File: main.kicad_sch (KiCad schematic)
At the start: 19 parts, among them J1 Conn_01x02_Pin, U1 LMC555xCMX, U2 LT8374RUFM-WPBF

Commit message: values
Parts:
- removed J1: Conn_01x02_Pin, symbol Connector:Conn_01x02_Pin
- added C10, C11, C8: C, symbol Device:C
- added C9: C_Polarized_US, symbol Device:C_Polarized_US
- added U3: TPS7B8133QDGNRQ1, VSSOP8_DGN_TEX, symbol _TPS7B81-Q1:TPS7B8133QDGNRQ1
- L1: value L -> 150 uH; Mfr (none) -> Bourns Inc.; Mfr P/N (none) -> SRN1060-151M; Supplier_1 (none) -> DigiKey; Supplier_1 P/N (none) -> SRN1060-151MCT-ND; Supplier_1 Price @ Qty (none) -> $0.67; Supplier_1 Unit Price (none) -> $0.67000
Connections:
- net GND: now also U2.8 (GND), C10.2, C11.2, C8.2, C9.2, U3.4 (GND), U3.5 (GND), U3.6 (GND), U3.9 (EPAD)
- net VIN: now also C8.1, C9.1
- net signal: now also U2.5 (CTRL)
- net DRV renamed +3V3
- net +3V3: now also C11.1, U3.8 (OUT)
- new net: C10.1, U3.1 (IN), U3.2 (EN)
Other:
- moved on the sheet: C1, C2, C3, C4, C5, C6, C7, D1, D2, D3, L1, R1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

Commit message: values, footprints, and part info complete
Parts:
- added C12: 1uF, Capacitor_SMD:C_0603_1608Metric, symbol Device:C
- added D4, D5: LED, _NavLights:LED_JB3030AWT_3X3_CRE, symbol Device:LED
- C1: value C -> 22nf; footprint (none) -> Capacitor_SMD:C_0805_2012Metric; Mfr (none) -> Murata Electronics; Mfr P/N (none) -> GCM21B5C1H223FA16L; Supplier_1 (none) -> DigiKey; Supplier_1 P/N (none) -> 490-GCM21B5C1H223FA16LCT-ND; Supplier_1 Price @ Qty (none) -> 1; Supplier_1 Unit Price (none) -> $0.52
- C10, C11, C8: value C -> 10uF; footprint (none) -> Capacitor_SMD:C_0805_2012Metric; Mfr (none) -> Murata Electronics; Mfr P/N (none) -> GRM21BR61H106KE43L; Supplier_1 (none) -> DigiKey; Supplier_1 P/N (none) -> 490-18663-1-ND; Supplier_1 Price @ Qty (none) -> 1; Supplier_1 Unit Price (none) -> $0.28
- C2, C4: footprint (none) -> Capacitor_SMD:C_0603_1608Metric; Mfr (none) -> KEMET; Mfr P/N (none) -> C0603C104K5RACTU; Supplier_1 (none) -> DigiKey; Supplier_1 P/N (none) -> 399-C0603C104K5RACTUCT-ND; Supplier_1 Price @ Qty (none) -> 1; Supplier_1 Unit Price (none) -> $0.08
- C3: value C -> 0.27; footprint (none) -> Capacitor_SMD:C_0805_2012Metric; Mfr (none) -> YAGEO; Mfr P/N (none) -> CC0805KKX7R9BB274; Supplier_1 (none) -> DigiKey; Supplier_1 P/N (none) -> 13-CC0805KKX7R9BB274CT-ND; Supplier_1 Price @ Qty (none) -> 1; Supplier_1 Unit Price (none) -> $0.20
- C5: value C -> 4.7uF; footprint (none) -> Capacitor_SMD:C_0805_2012Metric; Mfr (none) -> Murata Electronics; Mfr P/N (none) -> GRM21BR61H475KE51L; Supplier_1 (none) -> DigiKey; Supplier_1 P/N (none) -> 490-10751-1-ND; Supplier_1 Price @ Qty (none) -> 1; Supplier_1 Unit Price (none) -> $0.19
- C6: value C -> 47pF; footprint (none) -> Capacitor_SMD:C_0603_1608Metric; Mfr (none) -> Vishay Vitramon; Mfr P/N (none) -> VJ0603A470FXACW1BC; Supplier_1 (none) -> DigiKey; Supplier_1 P/N (none) -> 720-VJ0603A470FXACW1BCCT-ND; Supplier_1 Price @ Qty (none) -> 1; Supplier_1 Unit Price (none) -> $0.13
- C7: value C -> 2.2uF; footprint (none) -> Capacitor_SMD:C_0603_1608Metric; Mfr (none) -> Murata Electronics; Mfr P/N (none) -> GRM188R61H225KE11D; Supplier_1 (none) -> DigiKey; Supplier_1 P/N (none) -> 490-10733-1-ND; Supplier_1 Price @ Qty (none) -> 1; Supplier_1 Unit Price (none) -> $0.25
- C9: value C_Polarized_US -> 47uF; footprint (none) -> _NavLights:CAP_EEEFN2A100L; Mfr (none) -> Chemi-Con; Mfr P/N (none) -> HHXC500ARA470MHA0G; Supplier_1 (none) -> DigiKey; Supplier_1 P/N (none) -> 565-HHXC500ARA470MHA0GCT-ND; Supplier_1 Price @ Qty (none) -> 1; Supplier_1 Unit Price (none) -> $1.09
- D1, D2, D3: footprint (none) -> _NavLights:LED_JB3030AWT_3X3_CRE; Supplier_1 (none) -> DigiKey; Supplier_1 P/N (none) -> 2138-JB3030AWT-P-H65EA0000-N0000001CT-ND; Supplier_1 Price @ Qty (none) -> $0.69 for 10; Supplier_1 Unit Price (none) -> $0.10
- L1: value 150 uH -> 150uH; footprint (none) -> _NavLights:IND_BOURNS_SRN1060
- R1: value R_US -> 274kOhm; footprint (none) -> Resistor_SMD:R_0603_1608Metric; Mfr (none) -> Panasonic Electronic Components; Mfr P/N (none) -> ERA-3AEB2743V; Supplier_1 (none) -> DigiKey; Supplier_1 P/N (none) -> P274KDBCT-ND; Supplier_1 Price @ Qty (none) -> 1; Supplier_1 Unit Price (none) -> $0.10
- R2: value 1k -> 2490kOHm; footprint (none) -> Resistor_SMD:R_0603_1608Metric; Mfr (none) -> Stackpole Electronics Inc; Mfr P/N (none) -> RMCF0603FT2M49; Supplier_1 (none) -> DigKey; Supplier_1 P/N (none) -> RMCF0603FT2M49CT-ND; Supplier_1 Price @ Qty (none) -> 1; Supplier_1 Unit Price (none) -> $0.10
- R3: value R_US -> 100kOHm; footprint (none) -> Resistor_SMD:R_0603_1608Metric; Mfr (none) -> Stackpole Electronics Inc; Mfr P/N (none) -> RMCF0603FT100K; Supplier_1 (none) -> DigiKey; Supplier_1 P/N (none) -> RMCF0603FT100KCT-ND; Supplier_1 Price @ Qty (none) -> 1; Supplier_1 Unit Price (none) -> $0.10
- R4: value R_US -> 24mO; footprint (none) -> Resistor_SMD:R_0805_2012Metric; Mfr (none) -> Panasonic Electronic Components; Mfr P/N (none) -> ERJ-6CWDR024V; Supplier_1 (none) -> DigiKey; Supplier_1 P/N (none) -> P124410CT-ND; Supplier_1 Price @ Qty (none) -> 1; Supplier_1 Unit Price (none) -> $0.61
- R5: value R_US -> 10kO; footprint (none) -> Resistor_SMD:R_0603_1608Metric; Mfr (none) -> Panasonic Electronic Components; Mfr P/N (none) -> ERA-3AEB103V; Supplier_1 (none) -> DigiKey; Supplier_1 P/N (none) -> P10KDBCT-ND; Supplier_1 Price @ Qty (none) -> 1; Supplier_1 Unit Price (none) -> $0.10
- U2: Mfr (none) -> Analog Devices Inc.; Mfr P/N (none) -> LT8374RUFM#WPBF; Supplier_1 (none) -> DigiKey; Supplier_1 P/N (none) -> 505-LT8374RUFM#WPBF-ND; Supplier_1 Price @ Qty (none) -> 1; Supplier_1 Unit Price (none) -> $5.34
- U3: Mfr (none) -> Texas Instruments; Mfr P/N (none) -> TPS7B8133QDGNRQ1; Supplier_1 (none) -> DigiKey; Supplier_1 P/N (none) -> 296-TPS7B8133QDGNRQ1CT-ND; Supplier_1 Price @ Qty (none) -> 1; Supplier_1 Unit Price (none) -> $1.60
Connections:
- net GND: now also U2.17 (EPAD), C12.2, D5.1 (K)
- net INTVCC: now also U2.1 (SYNC/SPRD), U2.6 (CAP)
- net VIN: now also C10.1, U3.1 (IN), U3.2 (EN), C12.1
- net at D3.1 (K): now also D4.2 (A)
- new net: D4.1 (K), D5.2 (A)
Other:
- moved on the sheet: C1, C11, C2, C3, C4, C5, C6, C7, C8, C9, D1, L1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

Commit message: imprv to layout
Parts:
- added VIN: TestPoint, MountingHole:MountingHole_6mm_Pad_TopBottom, symbol Connector:TestPoint
- U3: footprint VSSOP8_DGN_TEX -> _NavLights:VSSOP8_DGN_TEX
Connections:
- net VIN: now also VIN.1
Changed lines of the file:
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@@
 			)
 		)
-		(property "Footprint" "VSSOP8_DGN_TEX"
+		(property "Footprint" "_NavLights:VSSOP8_DGN_TEX"
 			(at 58.42 48.26 0)
 			(effects
@@
 					(unit 1)
 				)
+			)
+		)
+	)
+	(symbol
+		(lib_id "Connector:TestPoint")
+		(at 231.14 125.73 0)
+		(unit 1)
+		(exclude_from_sim no)
+		(in_bom yes)
+		(on_board yes)
+		(dnp no)
+		(fields_autoplaced yes)
+		(property "Reference" "VIN"
+			(at 233.68 121.1579 0)
+			(effects
+				(font
+					(size 1.27 1.27)
+				)
+				(justify left)
+			)
+		)
+		(property "Value" "TestPoint"
+			(at 233.68 123.6979 0)
+			(effects
+				(font
+					(size 1.27 1.27)
+				)
+				(justify left)
+			)
+		)
+		(property "Footprint" "MountingHole:MountingHole_6mm_Pad_TopBottom"
+			(at 236.22 125.73 0)
+			(effects
+				(font
+					(size 1.27 1.27)
+				)
+				(hide yes)
+			)
+		)
+		(property "Datasheet" "~"
+			(at 236.22 125.73 0)
+			(effects
+				(font
+					(size 1.27 1.27)
+				)
+				(hide yes)
+			)
+		)
+		(property "Description" "test point"
+			(at 231.14 125.73 0)
+			(effects
+				(font
+					(size 1.27 1.27)
+				)
+				(hide yes)
+			)
+		)
+		(property "Mfr" ""
+			(at 231.14 125.73 0)
+			(effects
+				(font
+					(size 1.27 1.27)
+				)
+				(hide yes)
+			)
+		)
+		(property "Mfr P/N" ""
+			(at 231.14 125.73 0)
+			(effects
+				(font
+					(size 1.27 1.27)
+				)
+				(hide yes)
+			)
+		)
+		(property "Supplier_1" ""
+			(at 231.14 125.73 0)
+			(effects
+				(font
+					(size 1.27 1.27)
+				)
+				(hide yes)
+			)
+		)
+		(property "Supplier_1 P/N" ""
+			(at 231.14 125.73 0)
+			(effects
+				(font
+					(size 1.27 1.27)
+				)
+				(hide yes)
+			)
+		)
+		(property "Supplier_1 Price @ Qty" ""
+			(at 231.14 125.73 0)
+			(effects
+				(font
+					(size 1.27 1.27)
+				)
+				(hide yes)
+			)
+		)
+		(property "Supplier_1 Unit Price" ""
+			(at 231.14 125.73 0)
+			(effects
+				(font
+					(size 1.27 1.27)
+				)
+				(hide yes)
+			)
+		)
+		(property "Supplier_2" ""
+			(at 231.14 125.73 0)
+			(effects
+				(font
+					(size 1.27 1.27)
+				)
+				(hide yes)
+			)
+		)
+		(property "Supplier_2 P/N" ""
+			(at 231.14 125.73 0)
+			(effects
+				(font
+					(size 1.27 1.27)
+				)
+				(hide yes)
+			)
+		)
+		(property "Supplier_2 Price @ Qty" ""
+			(at 231.14 125.73 0)
+			(effects
+				(font
+					(size 1.27 1.27)
+				)
+				(hide yes)
+			)
+		)
+		(property "Supplier_2 Unit Price" ""
+			(at 231.14 125.73 0)
+			(effects
+				(font
+					(size 1.27 1.27)
+				)
+				(hide yes)
+			)
+		)
+		(pin "1"
+		)
+		(instances
+			(project ""
+				(path "/30b0ade0-bb43-474b-8aae-09f32d71430b/37ef2721-07c8-41aa-a59b-e8cb61a196fe"
+					(reference "VIN")
+					(unit 1)
+				)

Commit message: Touching up layout
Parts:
- removed VIN: TestPoint, MountingHole:MountingHole_6mm_Pad_TopBottom, symbol Connector:TestPoint
- added H5, H6: MountingHole_Pad, MountingHole:MountingHole_6mm_Pad_TopBottom, symbol Mechanical:MountingHole_Pad
- added TP1: TP_SIGNAL, _NavLights:HARWIN_S1751-46R, symbol Connector:TestPoint
- added TP2: TP_THR, _NavLights:HARWIN_S1751-46R, symbol Connector:TestPoint
- added TP3: 3V3, _NavLights:HARWIN_S1751-46R, symbol Connector:TestPoint
- added TP4: TP_GND, _NavLights:HARWIN_S1751-46R, symbol Connector:TestPoint
- added TP5: TP_ISN, _NavLights:HARWIN_S1751-46R, symbol Connector:TestPoint
- renumbered C10 to C1, C12 to C10, C8 to C11, C9 to C12, C11 to C5, C5 to C6, C6 to C7, C7 to C8, C1 to C9, R3 to R1, R1 to R3, R5 to R4, R4 to R5, U3 to U2, U2 to U3
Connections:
- net +3V3: now also TP3.1
- net GND: now also H5.1, TP4.1
- net ISN: now also TP5.1
- net THR: now also TP2.1
- net VIN: now also H6.1
- net signal: now also TP1.1

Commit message: optlayout
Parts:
- removed C2: 0.1uF, Capacitor_SMD:C_0603_1608Metric, symbol Device:C
- removed D5: LED, _NavLights:LED_JB3030AWT_3X3_CRE, symbol Device:LED
- removed U2: TPS7B8133QDGNRQ1, _NavLights:VSSOP8_DGN_TEX, symbol _TPS7B81-Q1:TPS7B8133QDGNRQ1
- added U2: TPS7B8133QWDRVRQ1, _NavLights:SON65P200X200X80-7N, symbol _TPS7B8133QWDRVRQ1(small):TPS7B8133DRVR
- D1, D2, D3, D4: footprint _NavLights:LED_JB3030AWT_3X3_CRE -> _NavLights:LED_0606 (M1616); Mfr P/N JB3030AWT-P-H65EA0000-N0000001 -> XQEAWT-00-0000-00000BG51; Supplier_1 P/N 2138-JB3030AWT-P-H65EA0000-N0000001CT-ND -> 90-XQEAWT-00-0000-00000BG51CT-ND; Supplier_1 Price @ Qty $0.69 for 10 -> 1; Supplier_1 Unit Price $0.10 -> $1.44000
- L1: value 150uH -> 22uH; footprint _NavLights:IND_BOURNS_SRN1060 -> _NavLights:IND_AMDLA4020S-220MT; Mfr Bourns Inc. -> Abracon LLC; Mfr P/N SRN1060-151M -> AMDLA4020S-220MT; Supplier_1 P/N SRN1060-151MCT-ND -> 535-AMDLA4020S-220MTCT-ND; Supplier_1 Price @ Qty $0.67 -> $0.83; Supplier_1 Unit Price $0.67000 -> $0.83000
- U1: value LMC555xCMX -> LMC555CMMX; Mfr P/N LMC555CMX/NOPB -> LMC555CMMX/NOPB; Supplier 1 P/N LMC555CMX/NOPBCT-ND -> LMC555CMMX/NOPBCT-ND; Supplier 1 Unit Price $1.10000 -> $1.26000
- U3: footprint 05-08-1799_ADI -> _NavLights:05-08-1799_ADI; Mfr P/N LT8374RUFM#WPBF -> LT8374RUFM-1#WPBF; Supplier_1 P/N 505-LT8374RUFM#WPBF-ND -> 505-LT8374RUFM-1#WPBF-ND; Supplier_1 Unit Price $5.34 -> $3.92000
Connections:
- net +3V3: now also U2.6 (OUT)
- net GND: now also D4.1 (K), U1.1 (GND), U2.3 (GND), U2.4 (GND), U2.7 (EXP)
- net VIN: now also U2.1 (IN), U2.2 (EN)
- no-connect marks 1 -> 2
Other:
- moved on the sheet: C1, C5, TP3, TP4

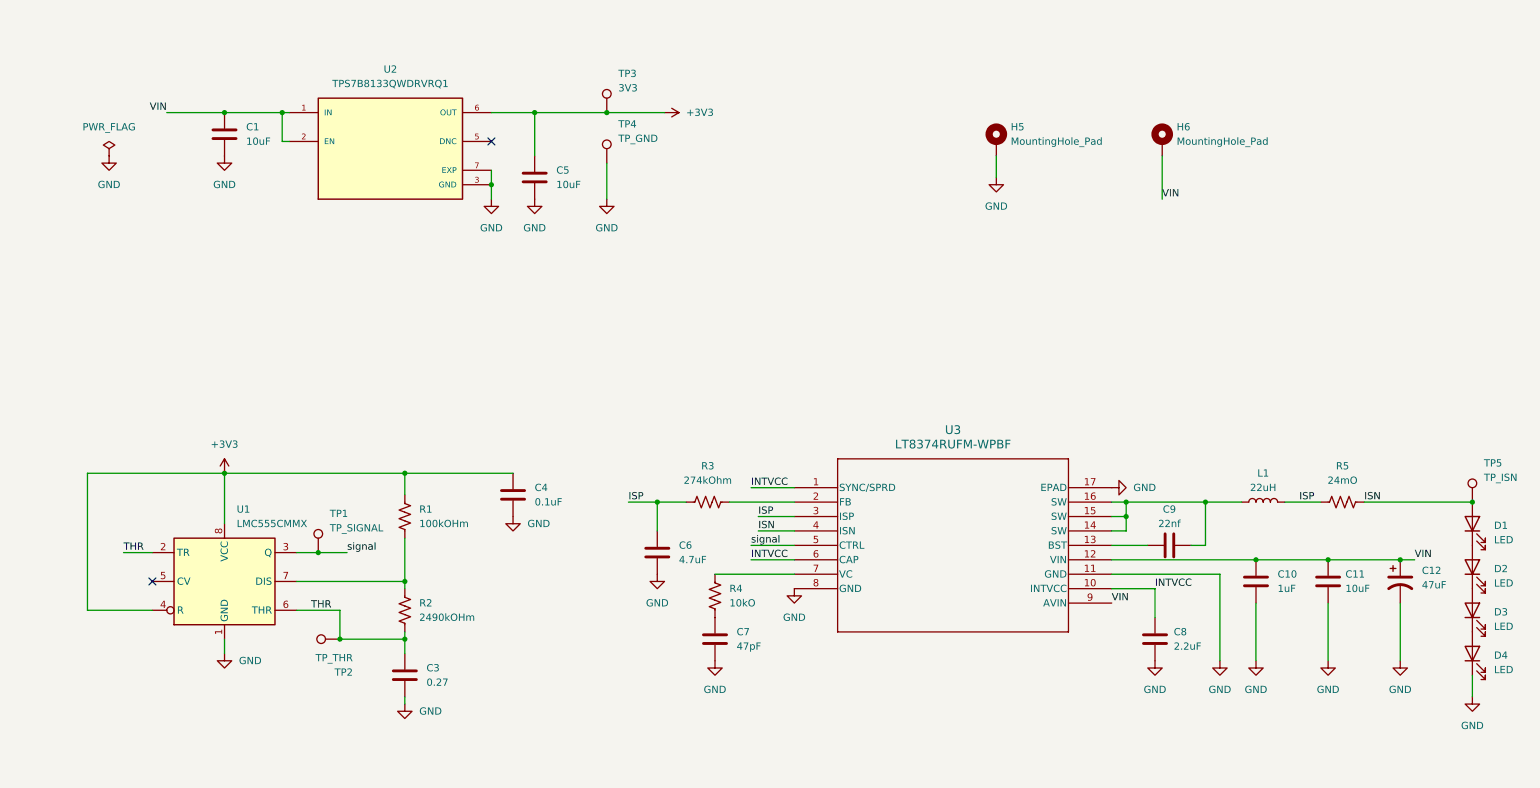
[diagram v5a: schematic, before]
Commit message: new opt layout
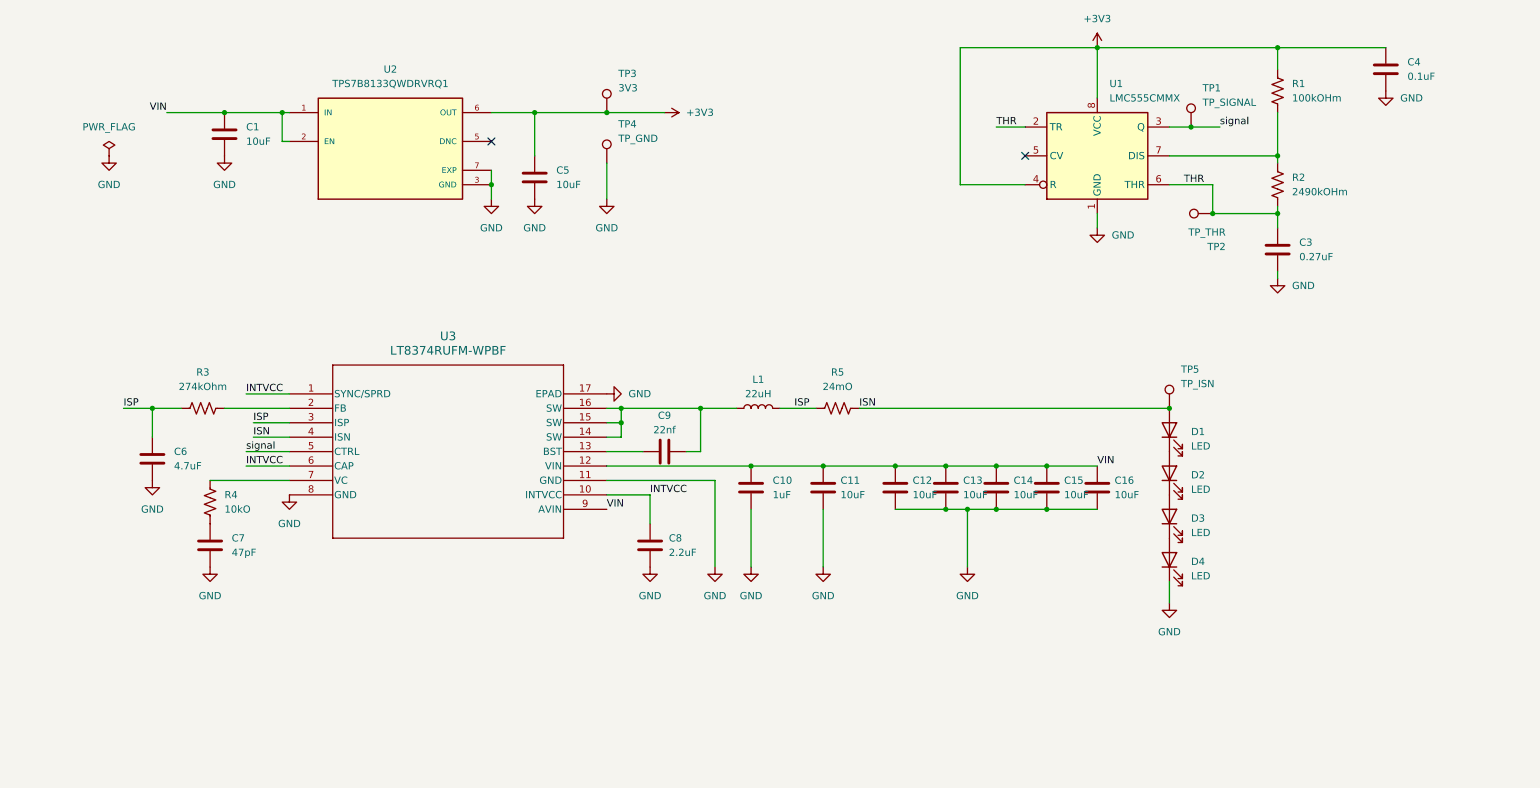
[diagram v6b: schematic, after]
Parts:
- removed C12: 47uF, _NavLights:CAP_EEEFN2A100L, symbol Device:C_Polarized_US
- removed H5, H6: MountingHole_Pad, MountingHole:MountingHole_6mm_Pad_TopBottom, symbol Mechanical:MountingHole_Pad
- added C12, C13, C14, C15, C16: 10uF, Capacitor_SMD:C_0805_2012Metric, symbol Device:C
- C3: value 0.27 -> 0.27uF
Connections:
- net GND: now also C12.2, C13.2, C14.2, C15.2, C16.2
- net VIN: now also C12.1, C13.1, C14.1, C15.1, C16.1
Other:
- moved on the sheet: C10, C11, C3, C4, C6, C7, C8, C9, D1, D2, D3, D4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

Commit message: Layout w/ connector
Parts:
- removed TP1: TP_SIGNAL, _NavLights:HARWIN_S1751-46R, symbol Connector:TestPoint
- removed TP2: TP_THR, _NavLights:HARWIN_S1751-46R, symbol Connector:TestPoint
- removed TP3: 3V3, _NavLights:HARWIN_S1751-46R, symbol Connector:TestPoint
- removed TP4: TP_GND, _NavLights:HARWIN_S1751-46R, symbol Connector:TestPoint
- removed TP5: TP_ISN, _NavLights:HARWIN_S1751-46R, symbol Connector:TestPoint
- added J1: Conn_01x02_Pin, Connector_AMASS:AMASS_XT30U-M_1x02_P5.0mm_Vertical, symbol Connector:Conn_01x02_Pin
- C4: footprint Capacitor_SMD:C_0603_1608Metric -> Capacitor_SMD:C_0402_1005Metric; Mfr KEMET -> Murata Electronics; Mfr P/N C0603C104K5RACTU -> GRM155C71H104JE19D; Supplier_1 P/N 399-C0603C104K5RACTUCT-ND -> 490-GRM155C71H104JE19DCT-ND; Supplier_1 Unit Price $0.08 -> $0.10
- C6: Mfr P/N GRM21BR61H475KE51L -> GRT21BC71H475KE13L; Supplier_1 P/N 490-10751-1-ND -> 490-GRT21BC71H475KE13LCT-ND; Supplier_1 Unit Price $0.19 -> $0.31
- C7: footprint Capacitor_SMD:C_0603_1608Metric -> Capacitor_SMD:C_0402_1005Metric; Mfr Vishay Vitramon -> Murata Electronics; Mfr P/N VJ0603A470FXACW1BC -> GCM1555C1H470FA16D; Supplier_1 P/N 720-VJ0603A470FXACW1BCCT-ND -> 490-16445-1-ND; Supplier_1 Unit Price $0.13 -> $0.10
- C9: footprint Capacitor_SMD:C_0805_2012Metric -> Capacitor_SMD:C_0402_1005Metric; Mfr P/N GCM21B5C1H223FA16L -> GRM155R71H223JA12D; Supplier_1 P/N 490-GCM21B5C1H223FA16LCT-ND -> 490-GRM155R71H223JA12DCT-ND; Supplier_1 Unit Price $0.52 -> $0.10
- R1: footprint Resistor_SMD:R_0603_1608Metric -> Resistor_SMD:R_0402_1005Metric; Mfr Stackpole Electronics Inc -> Vishay Dale; Mfr P/N RMCF0603FT100K -> TNPW0402100KBEED; Supplier_1 P/N RMCF0603FT100KCT-ND -> TNP100KDACT-ND; Supplier_1 Unit Price $0.10 -> $0.23
- R2: footprint Resistor_SMD:R_0603_1608Metric -> Resistor_SMD:R_0402_1005Metric; Mfr Stackpole Electronics Inc -> KOA Speer Electronics, Inc.; Mfr P/N RMCF0603FT2M49 -> RK73H1ETTP2494F; Supplier_1 DigKey -> DigiKey; Supplier_1 P/N RMCF0603FT2M49CT-ND -> 2019-RK73H1ETTP2494FCT-ND
- R3: footprint Resistor_SMD:R_0603_1608Metric -> Resistor_SMD:R_0402_1005Metric; Mfr Panasonic Electronic Components -> KOA Speer Electronics, Inc.; Mfr P/N ERA-3AEB2743V -> RK73H1ETTP2743F; Supplier_1 P/N P274KDBCT-ND -> 2019-RK73H1ETTP2743FCT-ND
- R4: footprint Resistor_SMD:R_0603_1608Metric -> Resistor_SMD:R_0402_1005Metric; Mfr Panasonic Electronic Components -> Vishay Dale; Mfr P/N ERA-3AEB103V -> TNPW040210K0BYEP; Supplier_1 P/N P10KDBCT-ND -> 541-4430-1-ND; Supplier_1 Unit Price $0.10 -> $0.49
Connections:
- net GND: now also J1.1 (Pin_1)
- net VIN: now also J1.2 (Pin_2)
